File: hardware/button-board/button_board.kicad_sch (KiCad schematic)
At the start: 15 parts, among them J1 Conn_01x05_Pin, SW1 RotaryEncoder_Switch, SW2 SW_Push, SW3 SW_Push, SW4 SW_Push, SW5 SW_Push, U1 MCP23S17_SP

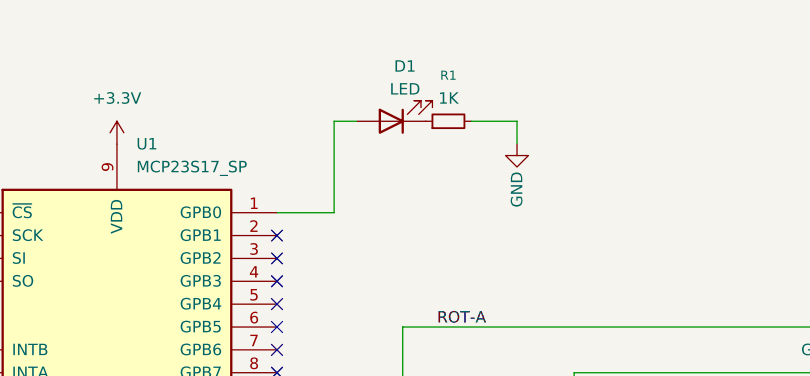
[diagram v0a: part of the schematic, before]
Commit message: Button board hardware design
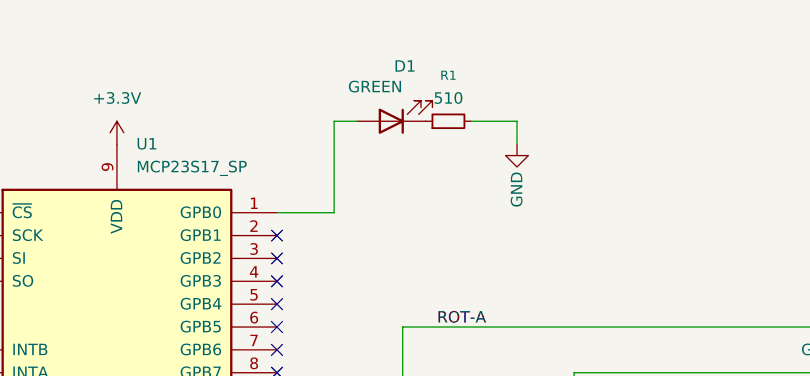
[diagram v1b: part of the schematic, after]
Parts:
- D1: value LED -> GREEN
- R1: value 1K -> 510
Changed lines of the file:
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@@
 			)
 		)
-		(property "Value" "LED"
-			(at 157.734 61.214 0)
+		(property "Value" "GREEN"
+			(at 154.432 60.96 0)
 			(effects
 				(font
@@
 			)
 		)
-		(property "Value" "1K"
+		(property "Value" "510"
 			(at 162.56 62.23 90)
 			(effects

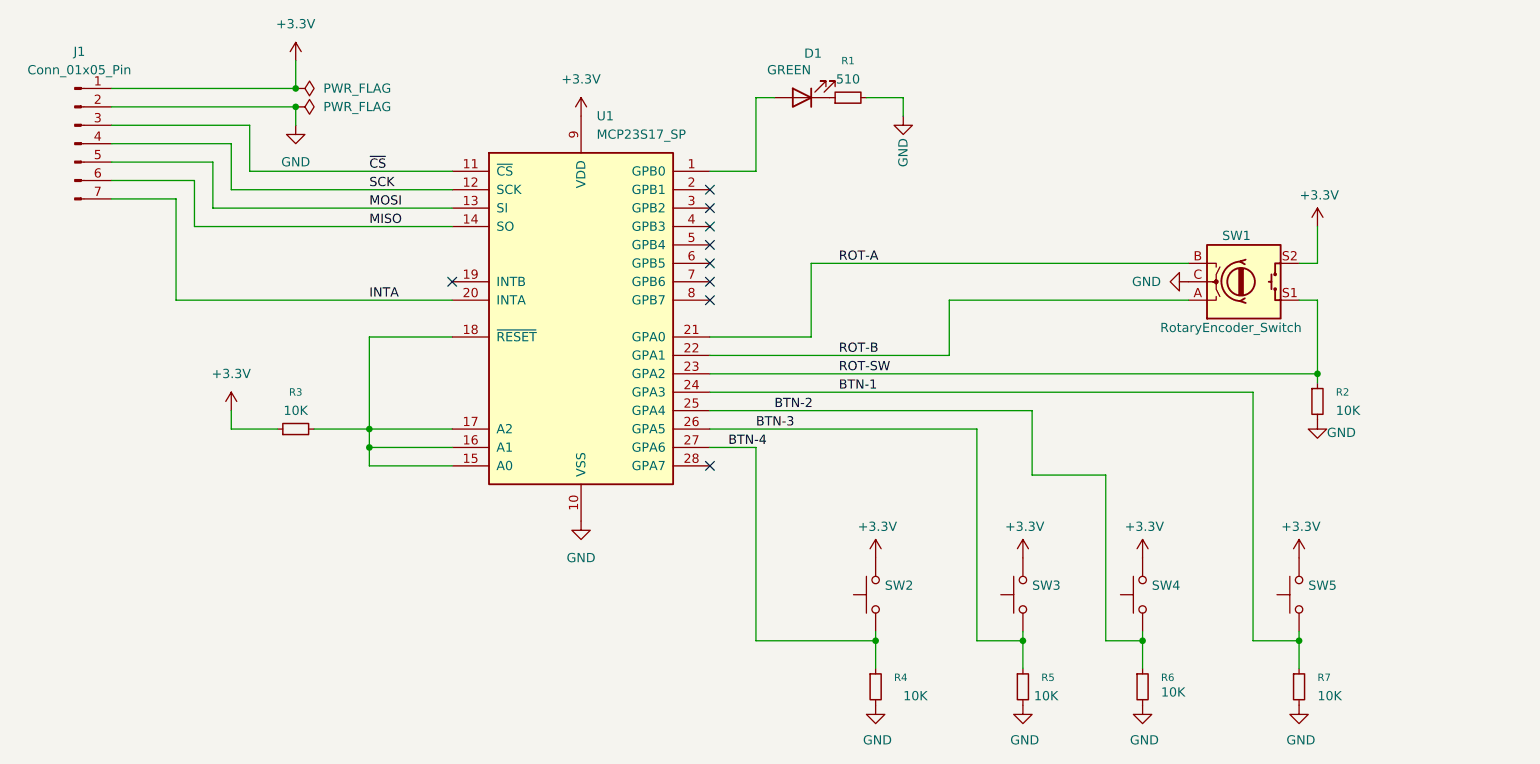
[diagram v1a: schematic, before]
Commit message: Preset buttons work (without interrupt logic)
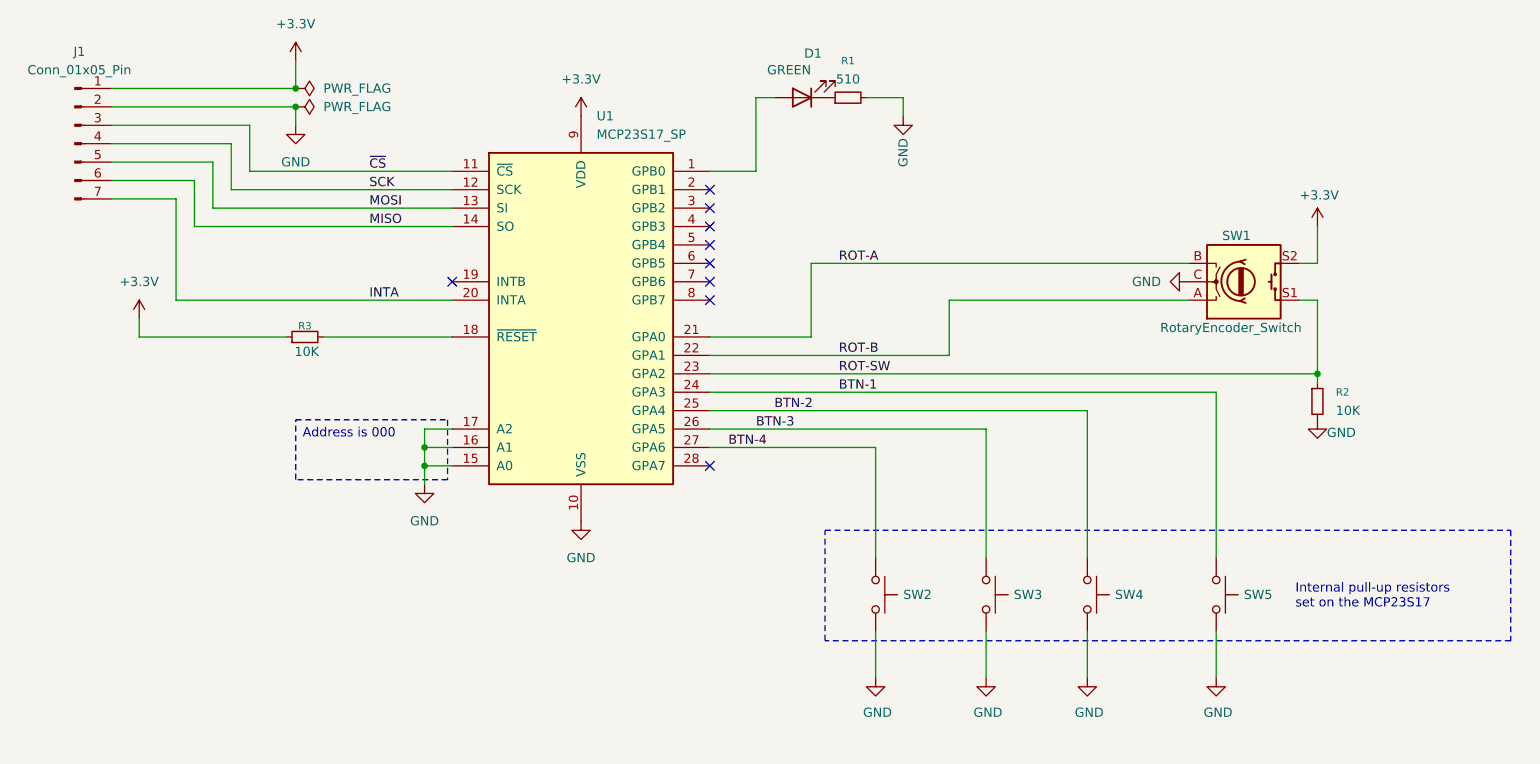
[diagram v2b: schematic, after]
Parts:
- removed R4, R5, R6, R7: 10K, Resistor_THT:R_Axial_DIN0207_L6.3mm_D2.5mm_P5.08mm_Vertical, symbol Device:R_Small
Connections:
- net +3.3V: no longer SW2.2, SW3.2, SW4.2, SW5.2
- net GND: now also SW2.2, SW3.2, SW4.2, SW5.2, U1.15 (A0), U1.16 (A1), U1.17 (A2)
- new net: R3.2, U1.18 (~{RESET})
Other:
- note added: "Internal pull-up resistors set on the MCP23S17"
- moved on the sheet: R3, SW2, SW3, SW4, SW5
